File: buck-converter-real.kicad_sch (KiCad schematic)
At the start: 37 parts, among them J1 SOLAR-IN, J6 BAT-OUT, Q2 CSD18540Q5B, U1 AP2112K-3.3, U5 LM5109BMA, U6 AS78L12RTR-G1

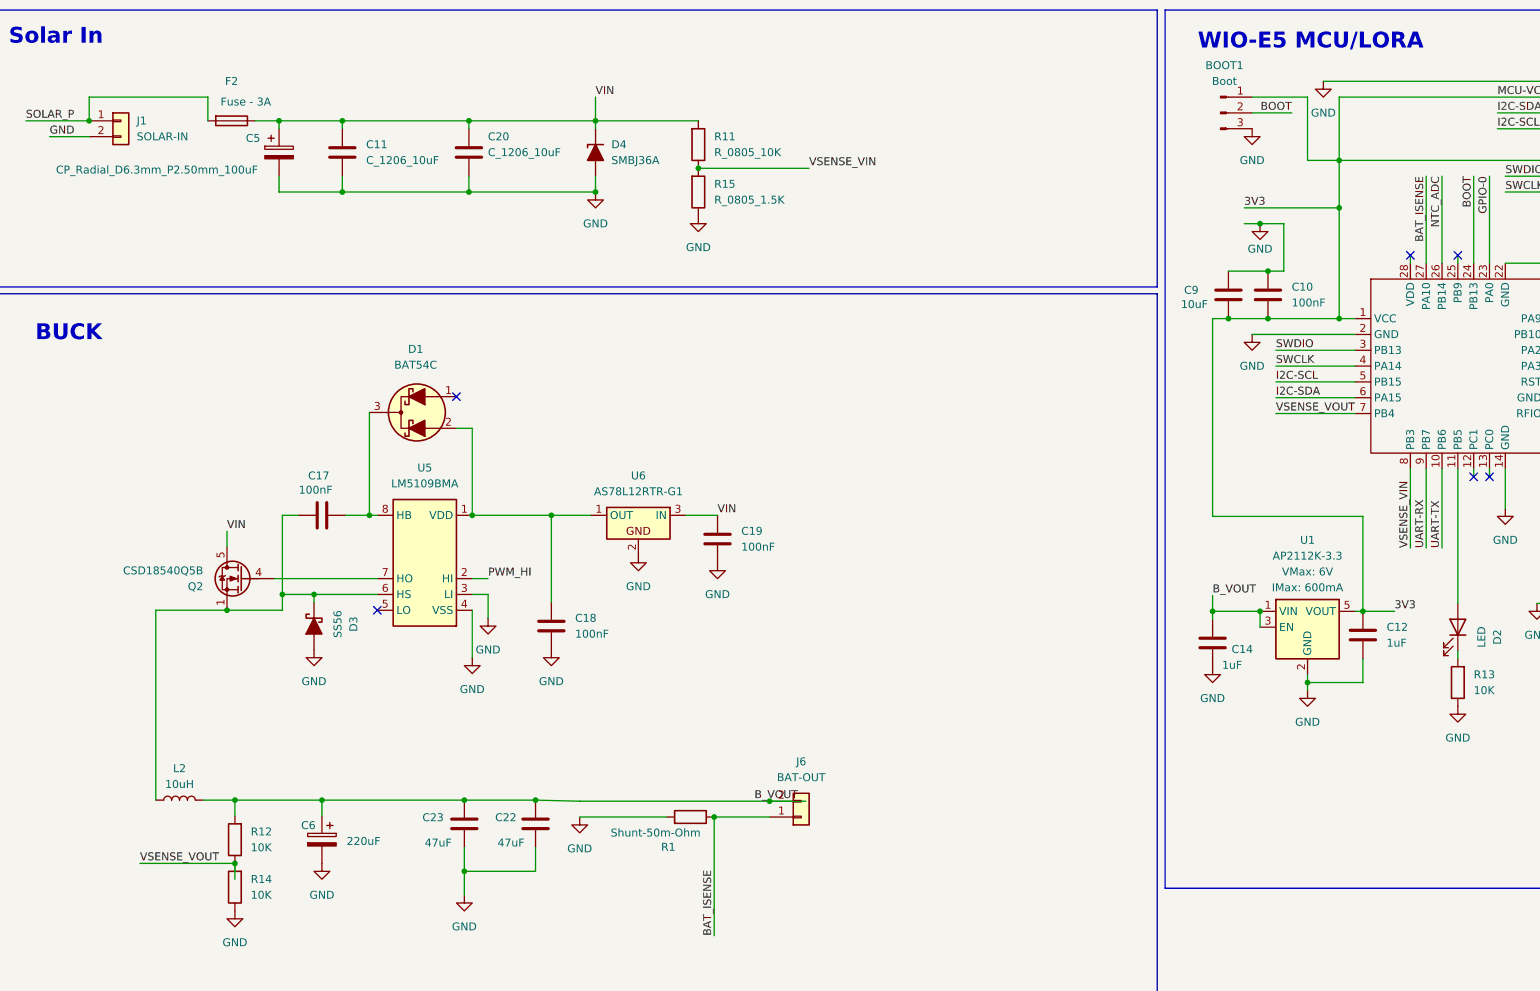
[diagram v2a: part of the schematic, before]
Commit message: Update PCB routing
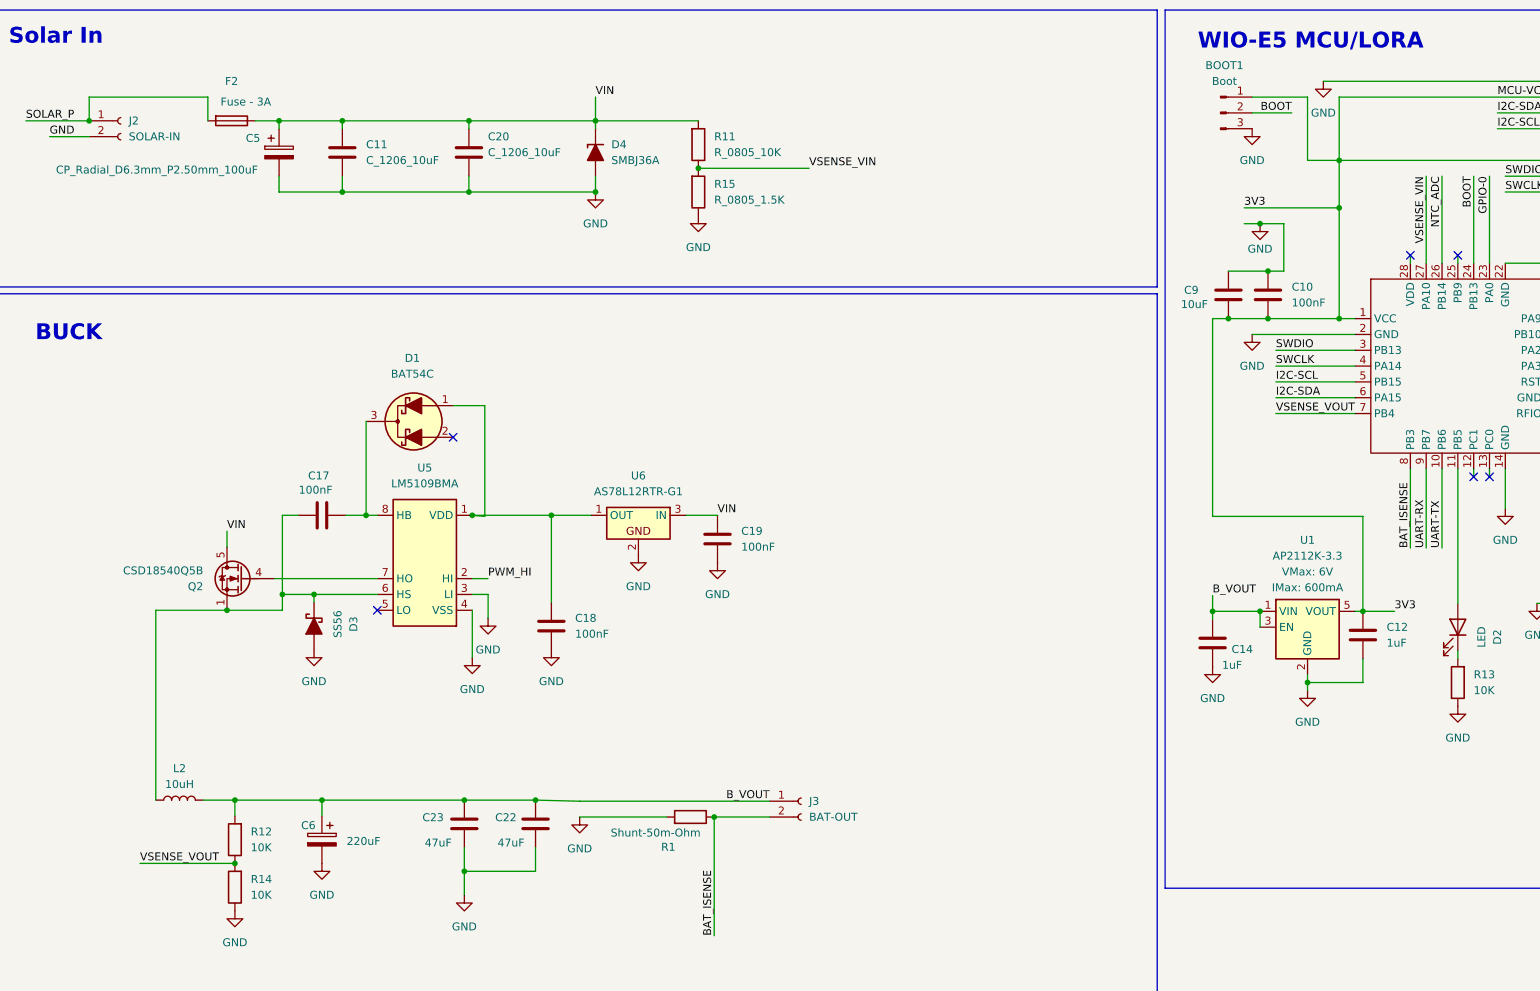
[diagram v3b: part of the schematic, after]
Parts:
- removed J1: SOLAR-IN, Connector_PinHeader_2.54mm:PinHeader_1x02_P2.54mm_Vertical, symbol Connector_Generic:Conn_01x02
- removed J6: BAT-OUT, Connector_PinHeader_2.54mm:PinHeader_1x02_P2.54mm_Vertical, symbol Connector_Generic:Conn_01x02
- added J2: SOLAR-IN, Connector_AMASS:AMASS_XT30UPB-F_1x02_P5.0mm_Vertical, symbol Connector:Conn_01x02_Socket
- added J3: BAT-OUT, Connector_AMASS:AMASS_XT30UPB-F_1x02_P5.0mm_Vertical, symbol Connector:Conn_01x02_Socket
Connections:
- net BAT_ISENSE: now also U3.8 (PB3), J3.2 (Pin_2); no longer U3.27 (PA10)
- net B_VOUT: now also J3.1 (Pin_1)
- net GND: now also J2.2 (Pin_2)
- net SOLAR_P: now also J2.1 (Pin_1)
- net VSENSE_VIN: now also U3.27 (PA10); no longer U3.8 (PB3)
- net at C18.1, U5.1 (VDD), U6.1 (OUT): now also D1.1 (A2); no longer D1.2 (A1)
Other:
- moved on the sheet: D1

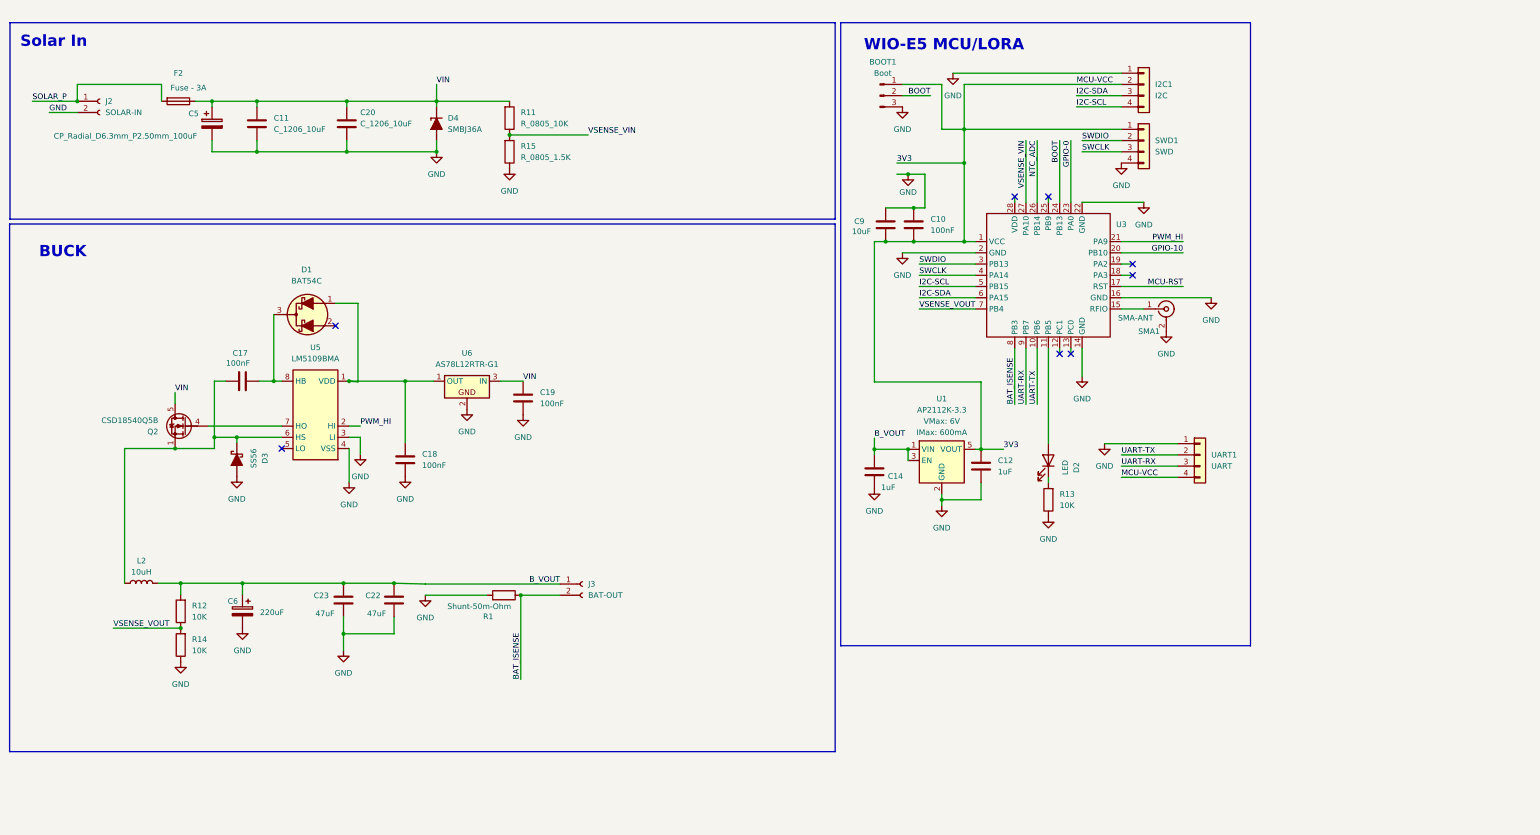
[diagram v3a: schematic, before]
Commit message: Update PCB routing
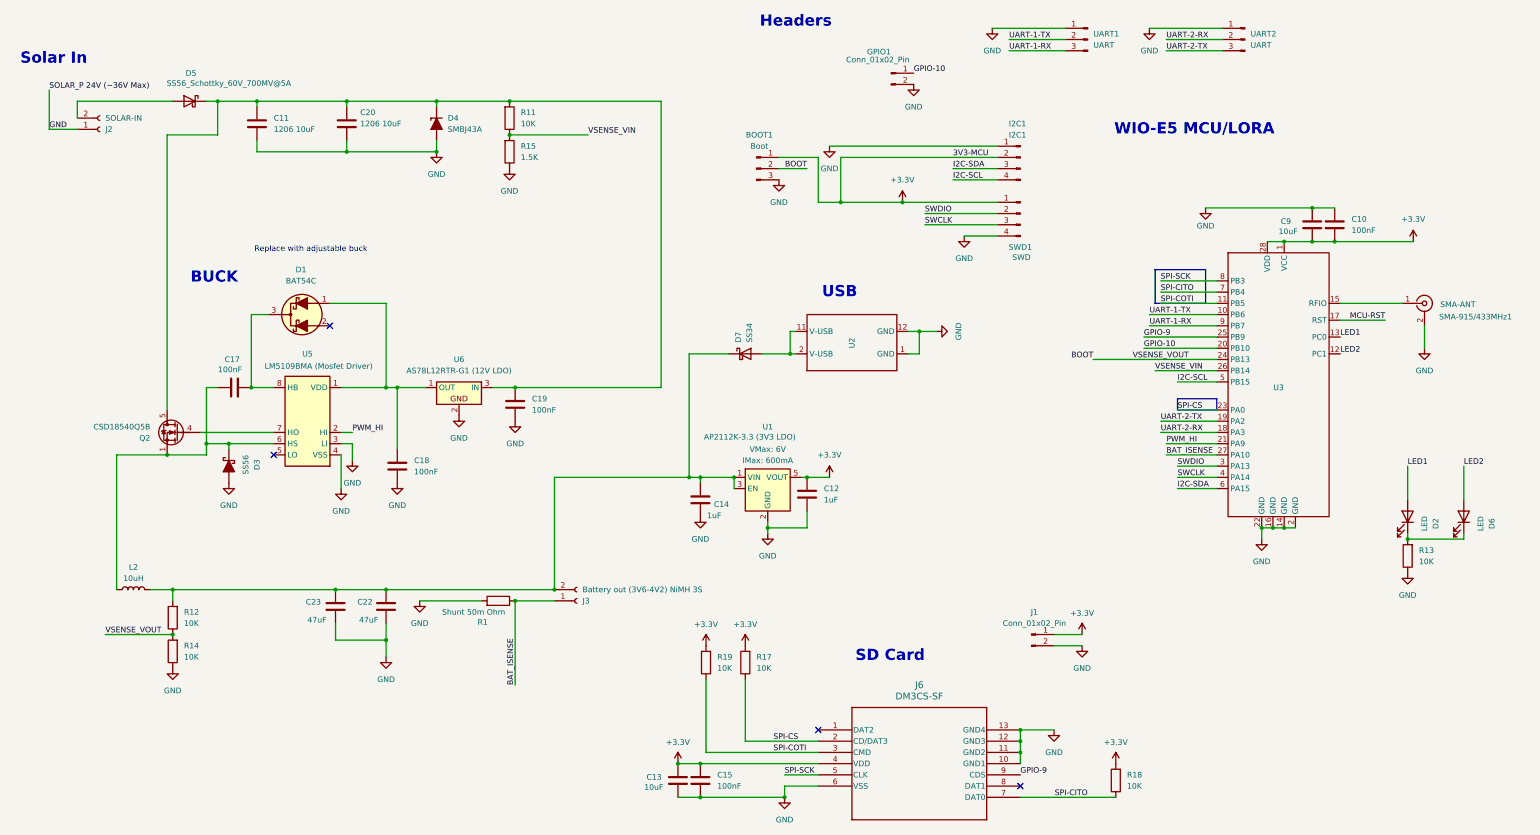
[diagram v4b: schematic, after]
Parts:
- removed C5: CP_Radial_D6.3mm_P2.50mm_100uF, PCM_Capacitor_THT_AKL:CP_Radial_D6.3mm_P2.50mm, symbol PCM_Capacitor_AKL:CP_Radial_D6.3mm_P2.50mm
- removed C6: 220uF, PCM_Capacitor_THT_AKL:CP_Radial_D6.3mm_P2.50mm, symbol PCM_Capacitor_AKL:CP_Radial_D6.3mm_P2.50mm
- removed F2: Fuse - 3A, Fuse:Fuse_1206_3216Metric, symbol Device:Fuse
- removed I2C1: I2C, Connector_PinSocket_2.54mm:PinSocket_1x04_P2.54mm_Vertical, symbol PCM_SparkFun-Connector:Conn_01x04_P2.54mm_Header_Horizontal_SMD
- removed SMA1: SMA-ANT, Connector_Coaxial:SMA_Samtec_SMA-J-P-H-ST-EM1_EdgeMount, symbol Connector:Conn_Coaxial
- removed SWD1: SWD, Connector_PinSocket_2.54mm:PinSocket_1x04_P2.54mm_Vertical, symbol PCM_SparkFun-Connector:Conn_01x04_P2.54mm_Header_Horizontal_SMD
- removed UART1: UART, Connector_PinSocket_2.54mm:PinSocket_1x04_P2.54mm_Vertical, symbol PCM_SparkFun-Connector:Conn_01x04_P2.54mm_Header_Horizontal_SMD
- added C13: 10uF, Capacitor_SMD:C_0603_1608Metric, symbol Device:C
- added C15: 100nF, Capacitor_SMD:C_0603_1608Metric, symbol Device:C
- added D5: SS56_Schottky_60V_700MV@5A, Diode_SMD:D_SMA, symbol Device:D_Schottky
- added D6: LED, LED_SMD:LED_0603_1608Metric_Pad1.05x0.95mm_HandSolder, symbol Device:LED
- added D7: SS34, Diode_SMD:D_SMA, symbol Diode:SS34
- added GPIO1, J1: Conn_01x02_Pin, Connector_PinHeader_2.54mm:PinHeader_1x02_P2.54mm_Vertical, symbol Connector:Conn_01x02_Pin
- added I2C1: I2C1, Connector_PinSocket_2.54mm:PinSocket_1x04_P2.54mm_Vertical, symbol Connector:Conn_01x04_Pin
- added J6: DM3CS-SF, Connector_Card:microSD_HC_Hirose_DM3D-SF, symbol 2026-05-05_06-59-55:DM3CS-SF
- added R17, R18, R19: 10K, PCM_Resistor_SMD_AKL:R_0805_2012Metric, symbol PCM_Resistor_AKL:R_0805
- added SMA-915/433MHz1: SMA-ANT, Connector_Coaxial:SMA_Samtec_SMA-J-P-H-ST-EM1_EdgeMount, symbol Connector:Conn_Coaxial
- added SWD1: SWD, Connector_PinSocket_2.54mm:PinSocket_1x04_P2.54mm_Vertical, symbol Connector:Conn_01x04_Pin
- added U2: (no value), buck-mppt:USB-CD16HMXTR, symbol buck-wio:USB-CD16HM
- added UART1, UART2: UART, Connector_PinSocket_2.54mm:PinSocket_1x03_P2.54mm_Vertical, symbol Connector:Conn_01x03_Pin
- C11, C20: value C_1206_10uF -> 1206 10uF
- D4: value SMBJ36A -> SMBJ43A; footprint Diode_THT:D_DO-201_P5.08mm_Vertical_CathodeUp -> Diode_SMD:D_SMB
- J3: value BAT-OUT -> Battery out (3V6-4V2) NiMH 3S
- R1: value Shunt-50m-Ohm -> Shunt 50m Ohm
- R11: value R_0805_10K -> 10K
- R15: value R_0805_1.5K -> 1.5K
- U1: value AP2112K-3.3 -> AP2112K-3.3 (3V3 LDO)
- U5: value LM5109BMA -> LM5109BMA (Mosfet Driver)
- U6: value AS78L12RTR-G1 -> AS78L12RTR-G1 (12V LDO)
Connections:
- net 3V3 is gone; now on net +3.3V: BOOT1.1 (Pin_1), C10.2, C12.1, C9.2, U1.5 (VOUT), U3.1 (VCC)
- net NTC_ADC is gone; now on net VSENSE_VIN: U3.26 (PB14)
- net SOLAR_P is gone; now on net GND: J2.1 (Pin_1)
- net BAT_ISENSE: now also J3.1 (Pin_1), U3.27 (PA10); no longer J3.2 (Pin_2), U3.8 (PB3)
- net BOOT: now also R12.2, R14.1
- net GND: now also C13.2, C15.2, GPIO1.2 (Pin_2), I2C1.1 (Pin_1), J1.2 (Pin_2), J6.10 (GND1), J6.11 (GND2), J6.12 (GND3), J6.13 (GND4), J6.6 (VSS), SMA-915/433MHz1.2 (Ext), SWD1.4 (Pin_4), U2.1 (GND), U2.12 (GND), UART1.1 (Pin_1), UART2.1 (Pin_1); no longer J2.2 (Pin_2)
- net GPIO-10: now also GPIO1.1 (Pin_1)
- net I2C-SCL: now also I2C1.4 (Pin_4)
- net I2C-SDA: now also I2C1.3 (Pin_3)
- net SWCLK: now also SWD1.3 (Pin_3)
- net SWDIO: now also SWD1.2 (Pin_2)
- net VSENSE_VIN: no longer U3.27 (PA10)
- net at D2.1 (K), R13.1: now also D6.1 (K)
- net LED1: now reaches D2.2 (A)
- net LED1: now also U3.13 (PC0); no longer U3.11 (PB5)
- net LED2: now reaches U3.12 (PC1)
- net LED2: now also D6.2 (A)
- net at U3.15 (RFIO): now also SMA-915/433MHz1.1 (In)
- net UART-2-RX: now reaches U3.18 (PA3)
- net UART-2-RX: now also UART2.2 (Pin_2)
- net UART-2-TX: now reaches U3.19 (PA2)
- net UART-2-TX: now also UART2.3 (Pin_3)
- net GPIO-9: now reaches U3.25 (PB9)
- net GPIO-9: now also J6.9 (CDS)
- net +3.3V: now reaches U3.28 (VDD)
- net +3.3V: now also C13.1, C15.1, I2C1.2 (Pin_2), J1.1 (Pin_1), J6.4 (VDD), R17.1, R18.1, R19.1, SWD1.1 (Pin_1)
- net B_VOUT: no longer names the net of C14.1, C22.1, C23.1, L2.1, R12.1, U1.1 (VIN), U1.3 (EN)
- net B_VOUT: now also J3.2 (Pin_2), D7.1 (K); no longer J3.1 (Pin_1)
- net GPIO-0 renamed SPI-CS
- net SPI-CS: now also J6.2 (CD/DAT3), R17.2
- net UART-RX renamed UART-1-RX
- net UART-1-RX: now also UART1.3 (Pin_3)
- net UART-TX renamed UART-1-TX
- net UART-1-TX: now also UART1.2 (Pin_2)
- net VIN: no longer names the net of C11.1, C19.1, C20.1, D4.1 (K), Q2.5 (D), R11.1, U6.3 (IN)
- net VIN: now also D5.1 (K)
- removed net VSENSE_VOUT: R12.2, R14.1, U3.7 (PB4)
- new net: D7.2 (A), U2.11 (V-USB), U2.2 (V-USB)
- new net: D5.2 (A), J2.2 (Pin_2)
- new net SPI-CITO: J6.7 (DAT0), R18.2, U3.7 (PB4)
- new net SPI-COTI: J6.3 (CMD), R19.2, U3.11 (PB5)
- new net SPI-SCK: J6.5 (CLK), U3.8 (PB3)
- no-connect marks 8 -> 4
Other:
- note added: "Headers"
- note added: "Replace with adjustable buck"
- note added: "SD Card"
- note added: "USB"
- moved on the sheet: BOOT1, C12, C14, C17, C18, C19, C22, C23, D1, D2, D3, J2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

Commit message: Update PCB routing
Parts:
- added C24: 47uF 10V 1206, PCM_Capacitor_SMD_AKL:C_1206_3216Metric, symbol PCM_Capacitor_AKL:C_1206
- added D8: SS34 - 40V 3A, Diode_SMD:D_SMA, symbol Diode:SS34
- added D9: SS56 60V 700MV@5A, PCM_Diode_SMD_AKL:D_SMC, symbol PCM_Diode_Schottky_AKL:SS56
- added J4: Conn_01x02, symbol Connector_Generic:Conn_01x02
- added L3: 10uH ±20% 18mΩ Molded, Inductor_SMD:L_10.4x10.4_H4.8, symbol Device:L
- added Q1: Q_NMOS_DGS, symbol Transistor_FET:Q_NMOS_DGS
- added Q3: Q_PMOS_DGS, symbol Transistor_FET:Q_PMOS_DGS
- added R16: 10K, PCM_Resistor_SMD_AKL:R_0805_2012Metric, symbol PCM_Resistor_AKL:R_0805
- added R20: 1k???, PCM_Resistor_SMD_AKL:R_0805_2012Metric, symbol PCM_Resistor_AKL:R_0805
- C10, C15, C17, C18, C19: value 100nF -> 100nF 50V
- C12, C14: value 1uF -> 1uF 25V
- C13, C9: value 10uF -> 10uF 50V
- C22, C23: value 47uF -> 47uF 10V 1206
- D3: value SS56 -> SS56 60V 700MV@5A
- D4: value SMBJ43A -> SMBJ43A - 43VWM 69.4VC
- D5: value SS56_Schottky_60V_700MV@5A -> SS56 60V 700MV@5A
- D7: value SS34 -> SS34 - 40V 3A
- J2: value SOLAR-IN -> XT60
- L2: value 10uH -> 10uH ±20% 18mΩ Molded
- Q2: value CSD18540Q5B -> CSD18540Q5B - 60-V
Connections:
- net GND: now also C24.2, D9.2 (A), Q1.3 (S), R16.2
- net +BATT: now reaches C22.1, C23.1, J3.2 (Pin_2), L2.1, R12.1
- net +BATT: now also D8.2 (A); no longer C14.1, D7.1 (K), U1.1 (VIN), U1.3 (EN)
- net at D2.1 (K), R13.1: no longer D6.1 (K)
- new net: C14.1, D7.1 (K), D8.1 (K), U1.1 (VIN), U1.3 (EN)
- new net: D6.1 (K), R16.1
- new net: Q1.1 (D), Q3.2 (G), R20.2
- new net: D9.1 (K), L3.2, Q3.1 (D)
- new net: Q3.3 (S), R20.1
- new net: C24.1, L3.1
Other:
- note added: "@ ??? mAnom"
- note added: "FIXME"
- note added: "LEDs"
- note added: "MPPT / Manual Buck"
- note added: "Maybe a LTC4411 "ideal" diode?"
- note added: "SOLAR-IN - 24V (~36V Max)"
- note added: "USBC?"
- note removed: "BUCK"
- moved on the sheet: BOOT1, C10, C11, C12, C13, C14, C15, C17, C18, C19, C20, C22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
